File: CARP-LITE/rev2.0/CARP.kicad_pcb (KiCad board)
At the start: 4 copper layers, 70.1 x 40 mm, 154 parts, among them J1 USB-C, J10 PYRO_2, J11 RF_L, J3 I2C1+3V3, J4 2S XT30, J5 UART+5V+I2C1, J6 PYRO_1, J7 RF_H, J8 PWM1+5V1, J9 PWM2+5V1, Q5 SQ2318CES, Q6 SQ2318CES, Q7 SQ2318CES, SW1 SW_Push, SW2 SW_Push, U1 W25Q128JVSIMTR (16MB), U10 TPS62130A, U2 W25Q32RVXHJQ (2MB), U4 RP2350_60QFN, U5 LSM6DSO, U6 BMP390, U7 TLV75733PDBV, U9 LR2021IMLTRT, Y1 ABM8-272-T3, Y2 ECS-TXO-25CSMV-320-AN-TR

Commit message: oops
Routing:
- net +3V3: track 28.4 -> 27.8 mm

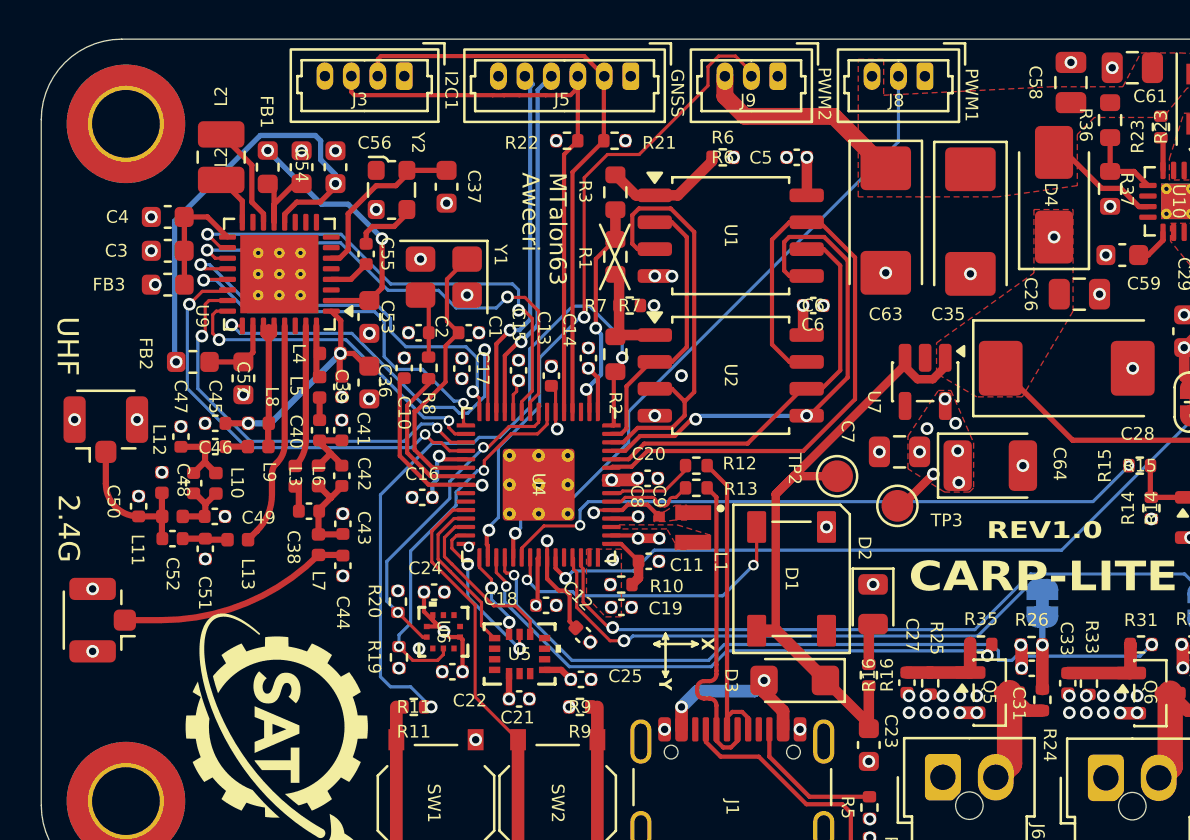
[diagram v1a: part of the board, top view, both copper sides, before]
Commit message: Move some of the vias out of the pads
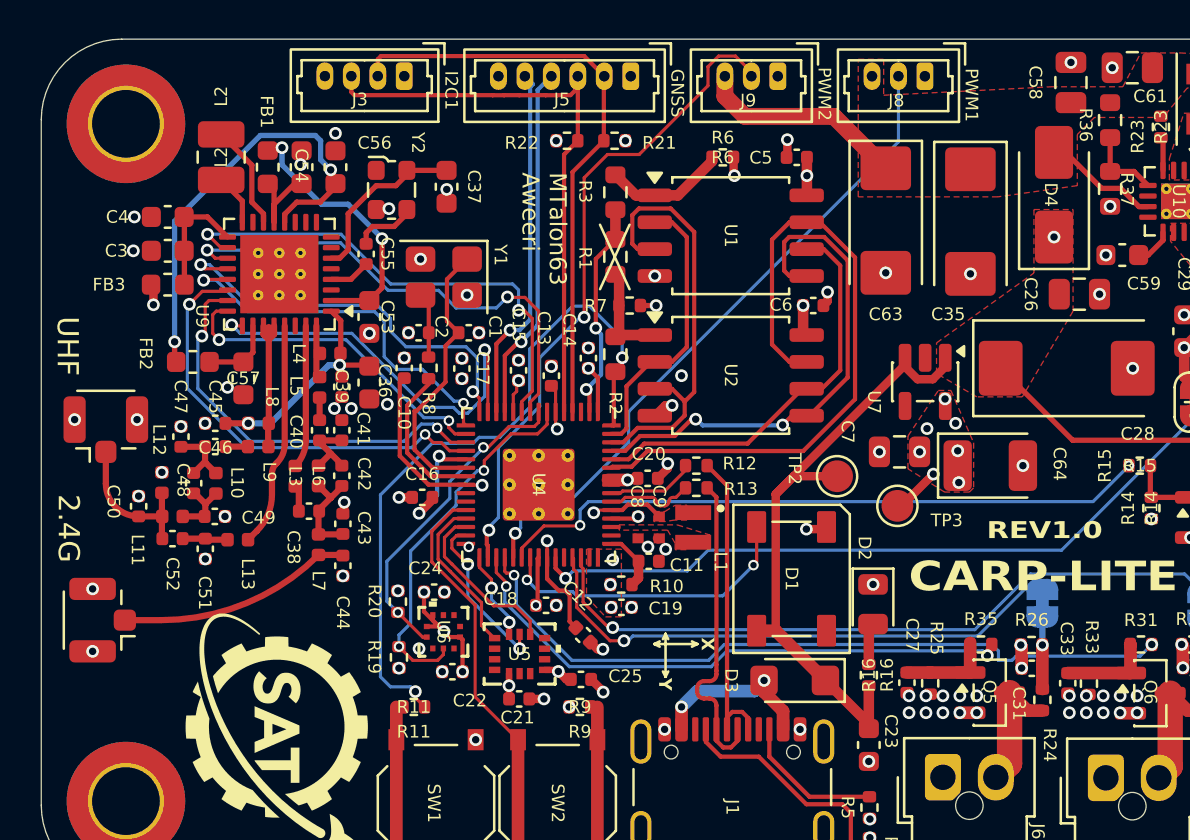
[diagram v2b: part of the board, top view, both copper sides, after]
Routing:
- net GND: track 4.55 -> 10.4 mm, vias 100 -> 98
- net +3V3: track 27.8 -> 32.5 mm, vias 34 -> 33
- net Net-(U9-VPAX2): track 12.1 -> 12.7 mm

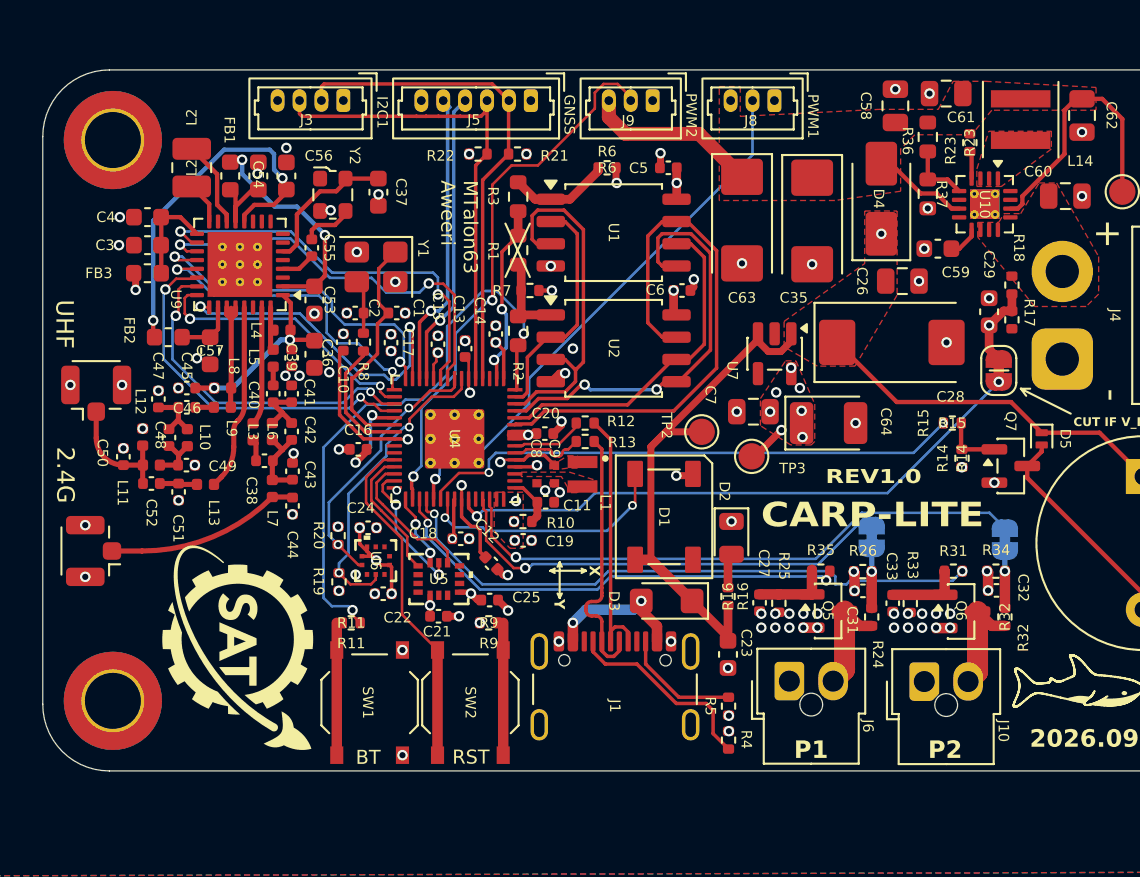
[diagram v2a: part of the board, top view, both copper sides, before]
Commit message: adjust silkscreen
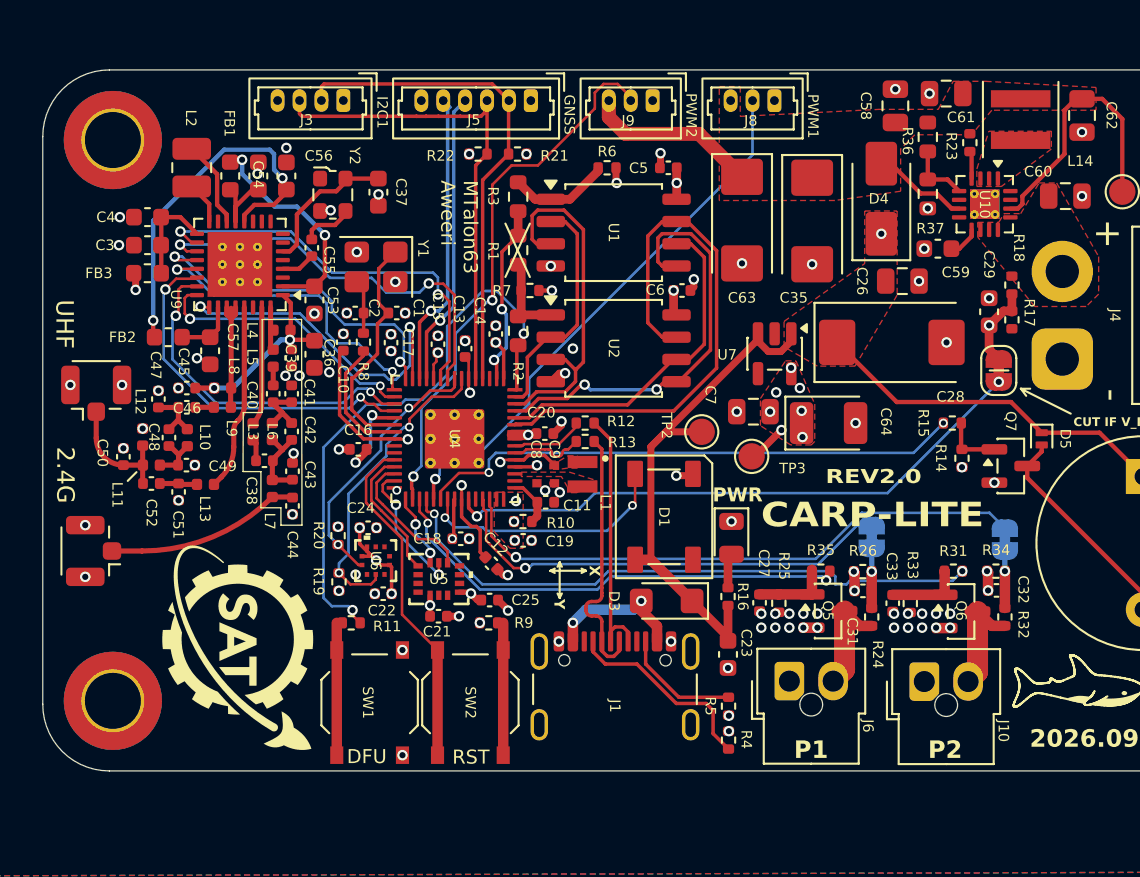
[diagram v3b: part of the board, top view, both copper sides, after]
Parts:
- renumbered D2 to PWR
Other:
- board text added: "DFU"
- board text added: "L2"
- board text added: "R14"
- board text added: "R15"
- board text added: "R16"
- board text added: "R23"
- board text added: "R32"
- board text added: "REV2.0"
- board text removed: "BT"
- board text removed: "REV1.0"
